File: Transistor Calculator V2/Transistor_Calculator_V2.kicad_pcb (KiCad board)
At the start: 2 copper layers, 95 x 60 mm, 61 parts, among them J1 5V, J2 GND, Q1 2N3904, Q10 2N3904, Q11 2N3904, Q12 2N3904, Q13 2N3904, Q14 2N3904, Q15 2N3904, Q16 2N3904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

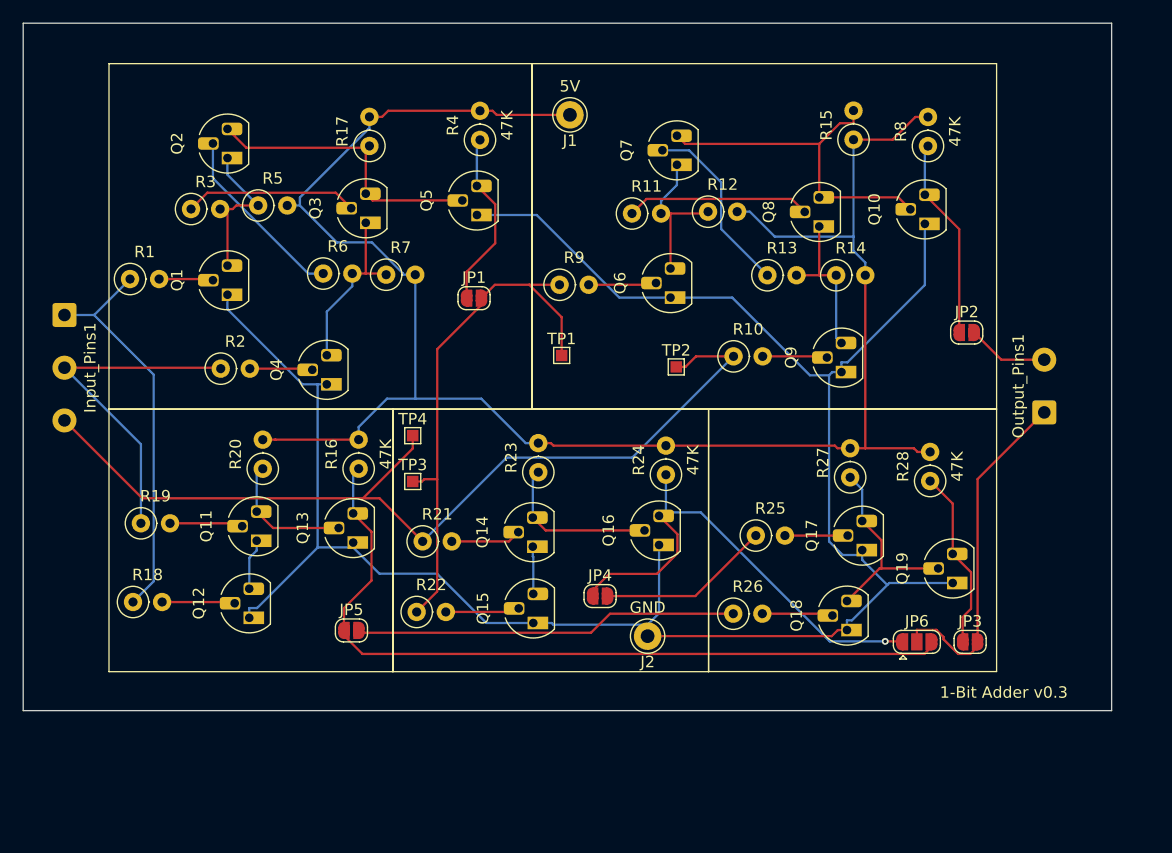
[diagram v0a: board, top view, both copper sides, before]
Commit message: Changes some routing. Added LED for debugging.
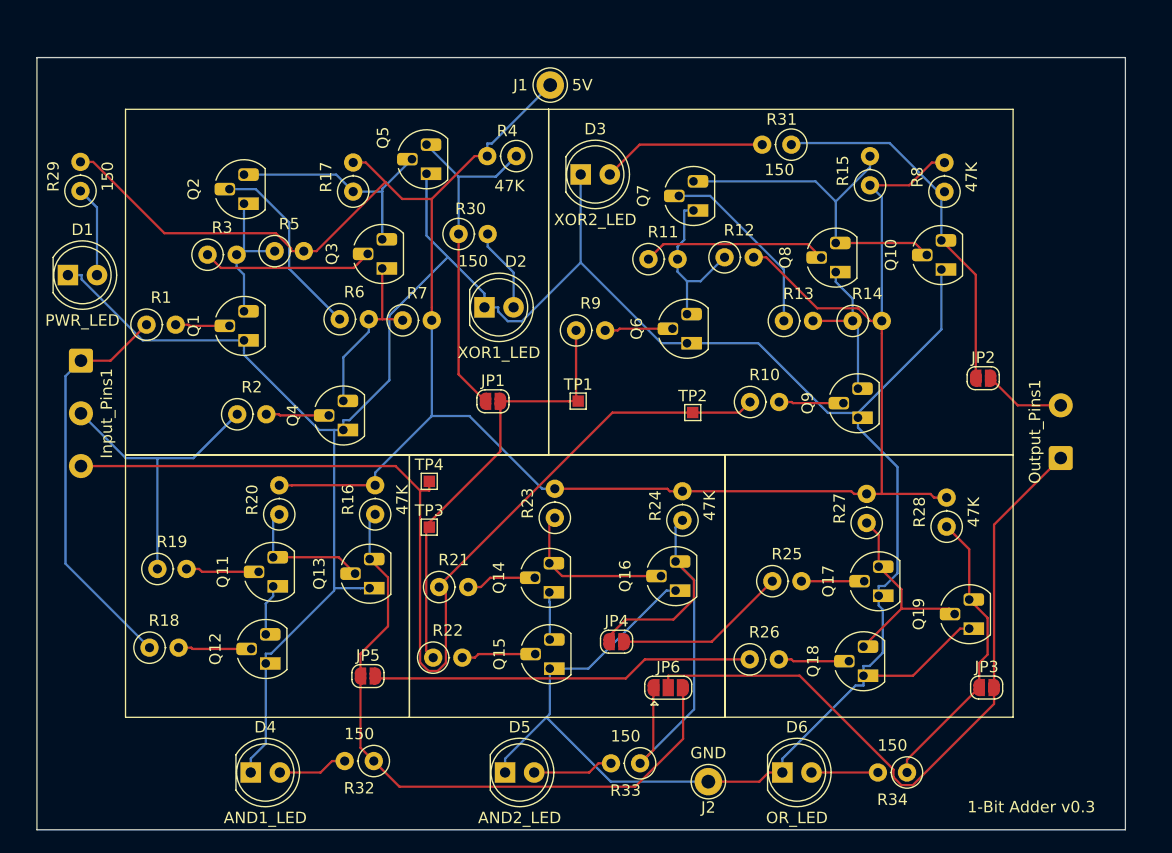
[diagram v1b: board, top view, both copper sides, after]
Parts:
- added D1: PWR_LED, LED_THT:LED_D5.0mm, F.Cu at (15.9, 34.0)
- added D2: XOR1_LED, LED_THT:LED_D5.0mm, F.Cu at (52.3, 36.8)
- added D3: XOR2_LED, LED_THT:LED_D5.0mm, F.Cu at (60.7, 25.2)
- added D4: AND1_LED, LED_THT:LED_D5.0mm, F.Cu at (31.9, 77.4)
- added D5: AND2_LED, LED_THT:LED_D5.0mm, F.Cu at (54.1, 77.4)
- added D6: OR_LED, LED_THT:LED_D5.0mm, F.Cu at (78.3, 77.4)
- added R29: 150, Resistor_THT:R_Axial_DIN0207_L6.3mm_D2.5mm_P2.54mm_Vertical, F.Cu at (17.0, 26.6)
- added R30: 150, Resistor_THT:R_Axial_DIN0207_L6.3mm_D2.5mm_P2.54mm_Vertical, F.Cu at (50.0, 30.4)
- added R31: 150, Resistor_THT:R_Axial_DIN0207_L6.3mm_D2.5mm_P2.54mm_Vertical, F.Cu at (79.0, 22.6)
- added R32: 150, Resistor_THT:R_Axial_DIN0207_L6.3mm_D2.5mm_P2.54mm_Vertical, F.Cu at (42.6, 76.4)
- added R33: 150, Resistor_THT:R_Axial_DIN0207_L6.3mm_D2.5mm_P2.54mm_Vertical, F.Cu at (65.8, 76.6)
- added R34: 150, Resistor_THT:R_Axial_DIN0207_L6.3mm_D2.5mm_P2.54mm_Vertical, F.Cu at (89.1, 77.4)
- moved JP6 22.1 mm to (68.3, 70.0)
- moved J2 13.8 mm to (71.8, 78.2)
- moved JP1 9.15 mm to (53.0, 45.0)
- moved Q5 5.69 mm to (47.2, 25.1)
- moved R24 4.24 mm to (69.5, 55.4)
- moved R25 4.24 mm to (77.4, 60.7)
- moved JP5 4.24 mm to (42.1, 69.0)
- moved Q13 4.24 mm to (42.2, 61.3)
- moved Q14 4.24 mm to (57.9, 61.7)
- moved R9 4.24 mm to (60.3, 38.8)
- moved R1 4.24 mm to (22.8, 38.3)
- moved R19 4.24 mm to (23.7, 59.6)
- moved R2 4.24 mm to (30.7, 46.1)
- moved R3 4.24 mm to (28.1, 32.2)
- moved Input_Pins1 4.24 mm to (17.0, 41.5)
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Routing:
- net Net-(D1-K): track 181.2 -> 260.9 mm
- net Net-(JP3-B): track 30.5 -> 60.6 mm
- net Net-(J1-Pin_1): track 160.8 -> 187.3 mm
- net Net-(JP2-A): track 17.6 -> 32.7 mm
- net Net-(JP1-A): track 15.6 -> 30.3 mm
- net Net-(D3-A): track 0.00 -> 14.4 mm
- net Net-(JP5-A): track 69.1 -> 58.0 mm
- net Net-(JP3-A): track 15.8 -> 25.8 mm
- net Net-(Input_Pins1-Pin_3): track 82.1 -> 90.8 mm
- net Net-(D1-A): track 0.00 -> 7.94 mm
- net Net-(JP1-B): track 46.6 -> 38.8 mm
- net Net-(D2-A): track 0.00 -> 7.34 mm
- net Net-(D5-A): track 0.00 -> 7.04 mm
- net Net-(D4-A): track 0.00 -> 6.07 mm
- net Net-(D6-A): track 0.00 -> 5.80 mm
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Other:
- board size 95 x 60 mm -> 95 x 67.4 mm

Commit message: Small changes
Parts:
- added J3: 5V_Out, Connector_Pin:Pin_D1.0mm_L10.0mm_LooseFit, F.Cu at (66.8, 16.8)
- added J4: GND_Out, Connector_Pin:Pin_D1.0mm_L10.0mm_LooseFit, F.Cu at (17.0, 76.8)
- J1: value 5V -> 5V_In
- J2: value GND -> GND_In
- moved J2 55.7 mm to (17.2, 67.2)
- moved J1 8.21 mm to (49.8, 17.0)
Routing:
- net Net-(D1-K): track 260.9 -> 295.4 mm
- net Net-(J1-Pin_1): track 187.3 -> 205.5 mm
- net Net-(Q2-B): track 16.7 -> 18.7 mm

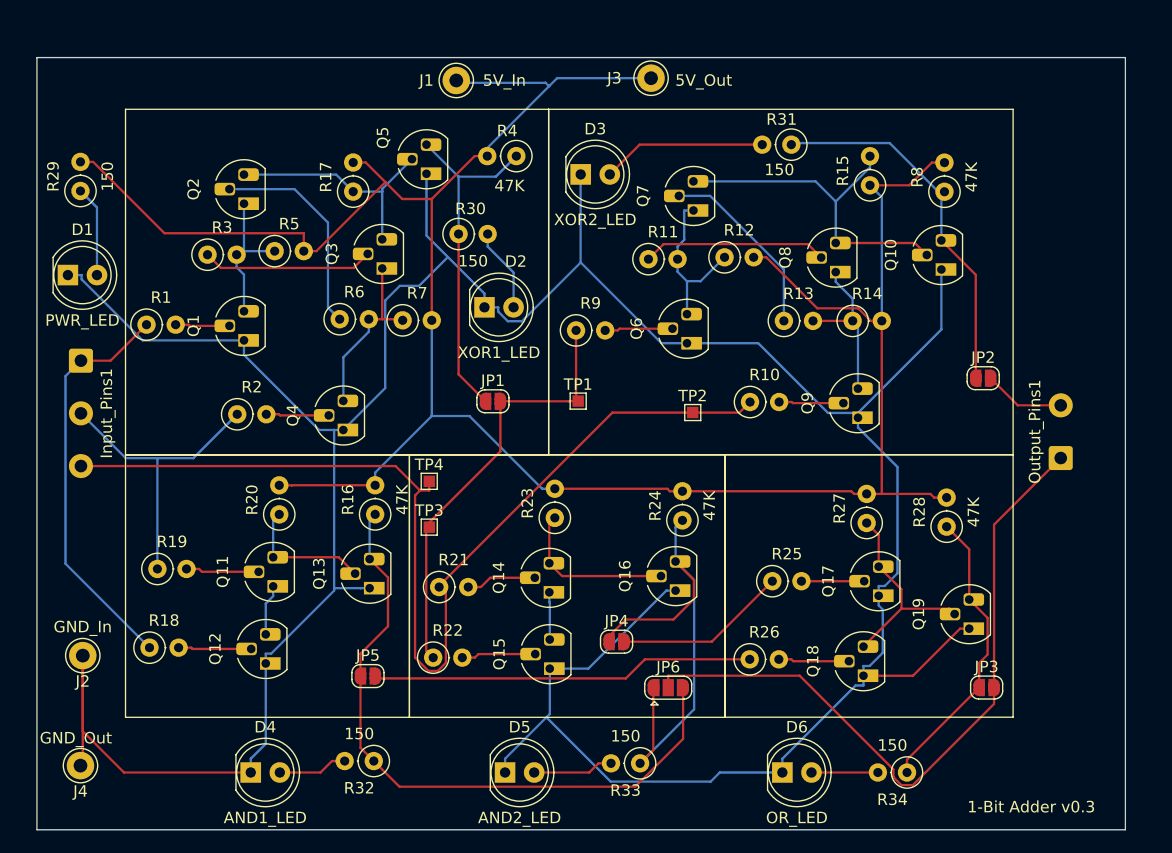
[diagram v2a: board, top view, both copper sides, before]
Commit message: Added diode and changes some of the pcb placements
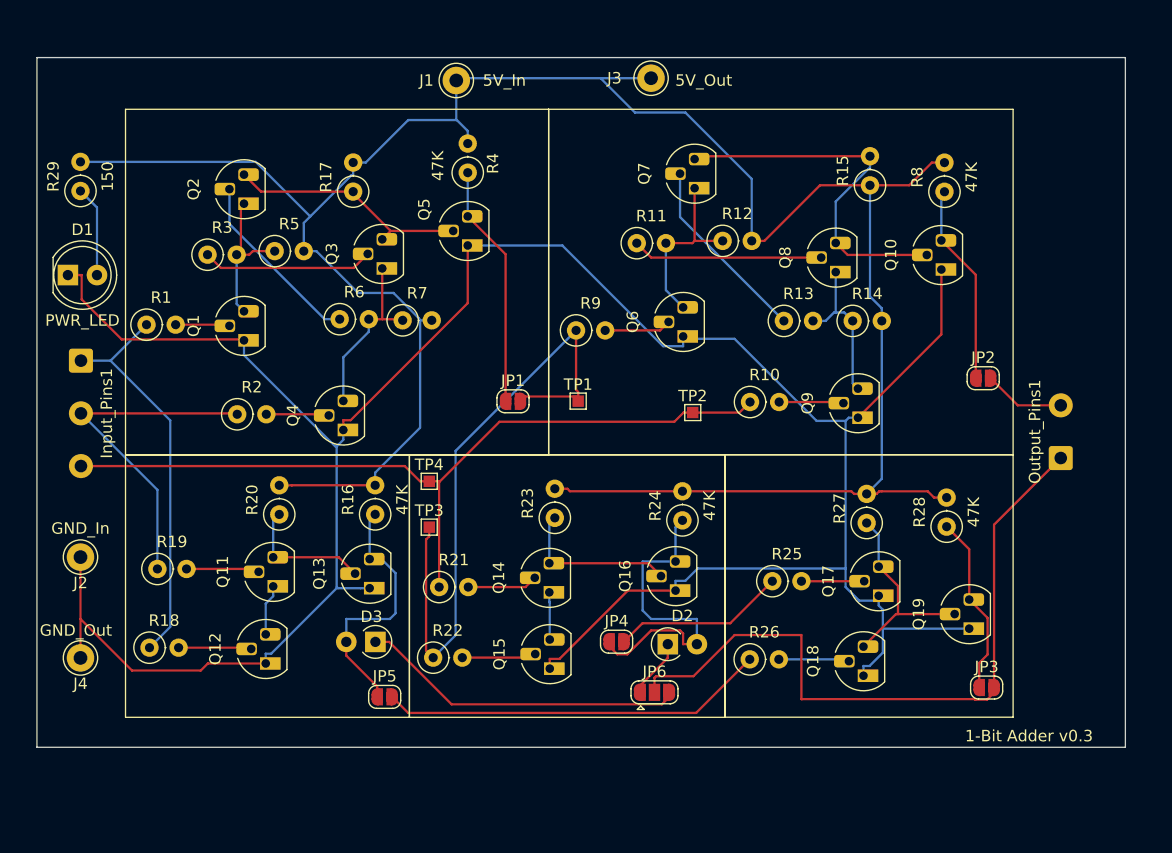
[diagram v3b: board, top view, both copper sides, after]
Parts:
- removed D4: AND1_LED, LED_THT:LED_D5.0mm
- removed D5: AND2_LED, LED_THT:LED_D5.0mm
- removed D6: OR_LED, LED_THT:LED_D5.0mm
- removed R30, R31, R32, R33, R34: 150, Resistor_THT:R_Axial_DIN0207_L6.3mm_D2.5mm_P2.54mm_Vertical
- D2: value XOR1_LED -> D; footprint LED_THT:LED_D5.0mm -> Diode_THT:D_A-405_P2.54mm_Vertical_AnodeUp
- D3: value XOR2_LED -> D; footprint LED_THT:LED_D5.0mm -> Diode_THT:D_A-405_P2.54mm_Vertical_AnodeUp
- moved D3 44.6 mm to (42.7, 66.0), turned to 180 degrees
- moved D2 33.5 mm to (68.3, 66.2)
- moved J4 9.40 mm to (17.0, 67.4)
- moved J2 8.60 mm to (17.0, 58.6)
- moved Q5 7.22 mm to (50.8, 31.4)
- moved R4 4.48 mm to (50.8, 25.0), turned to 90 degrees
- moved JP5 2.33 mm to (43.5, 70.8)
- moved Q7 1.95 mm to (70.6, 26.4)
- moved JP1 1.75 mm to (54.8, 45.0)
- moved R11 1.73 mm to (65.6, 31.2)
- moved R12 1.44 mm to (73.0, 31.0)
- moved JP6 1.26 mm to (67.1, 70.4)
- moved Q6 0.68 mm to (69.6, 39.3)
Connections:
- D2 pad 1: Net-(D1-K) -> Net-(D2-K)
- D3 pad 1: Net-(D1-K) -> Net-(D3-K)
- JP4 pad 1: Net-(JP4-A) -> Net-(D2-A)
- JP5 pad 1: Net-(JP5-A) -> Net-(D3-A)
- JP6 pad 1: Net-(JP4-A) -> Net-(D2-K)
- JP6 pad 3: Net-(JP5-A) -> Net-(D3-K)
- Q13 pad 3: Net-(JP5-A) -> Net-(D3-A)
- Q16 pad 3: Net-(JP4-A) -> Net-(D2-A)
- R16 pad 1: Net-(JP5-A) -> Net-(D3-A)
- R24 pad 1: Net-(JP4-A) -> Net-(D2-A)
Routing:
- net Net-(D1-K): track 295.4 -> 229.1 mm
- net Net-(JP5-A): track 58.0 -> 0.00 mm
- net Net-(JP4-A): track 44.3 -> 0.00 mm
- net Net-(D3-K): track 0.00 -> 28.6 mm
- net Net-(D2-A): track 7.34 -> 28.5 mm
- net Net-(Input_Pins1-Pin_3): track 91.1 -> 71.0 mm
- net Net-(JP1-B): track 38.8 -> 56.9 mm
- net Net-(JP2-A): track 32.7 -> 17.6 mm
- net Net-(JP3-A): track 25.8 -> 15.8 mm
- net Net-(JP1-A): track 30.3 -> 21.3 mm
- net Net-(D3-A): track 14.4 -> 22.8 mm
- net Net-(D5-A): track 7.04 -> 0.00 mm
- net Net-(D4-A): track 6.07 -> 0.00 mm
- net Net-(D6-A): track 5.80 -> 0.00 mm
- net Net-(D2-K): track 0.00 -> 5.22 mm
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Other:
- board size 95 x 67.4 mm -> 95 x 60.2 mm
